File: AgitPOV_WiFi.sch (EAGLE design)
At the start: 43 parts, among them U1 MMA8452Q

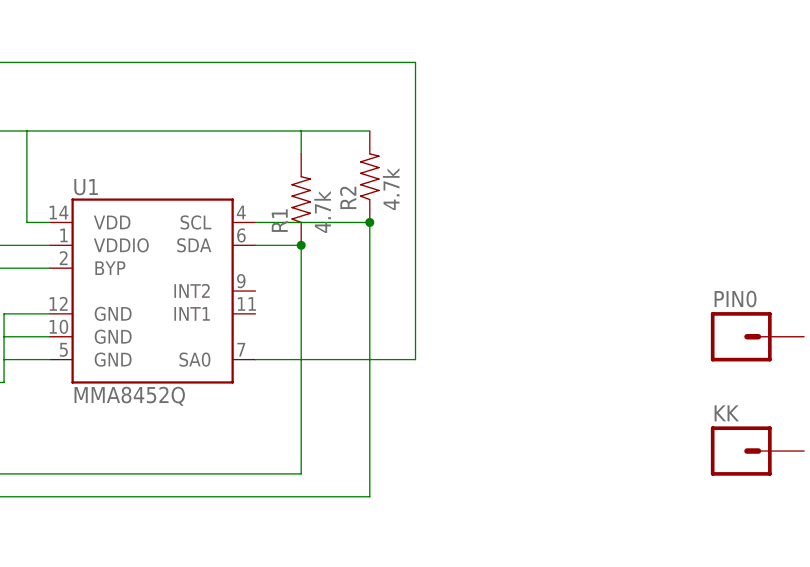
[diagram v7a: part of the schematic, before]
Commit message: Added pin headers for INT1 and INT2
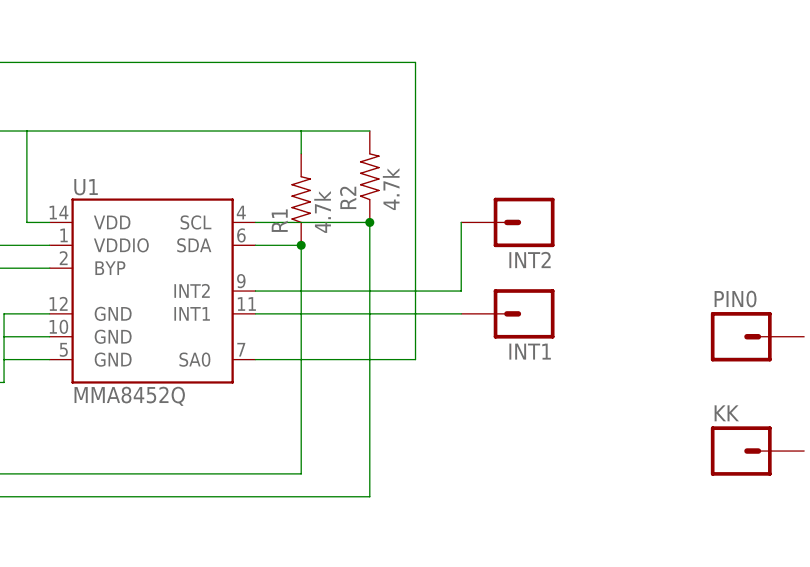
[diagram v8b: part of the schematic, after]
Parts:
- added INT1, INT2: (no value), SparkFun-Connectors:M01PTH
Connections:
- new net N$65: INT1.1, U1.INT1
- new net N$67: INT2.1, U1.INT2
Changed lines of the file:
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@@
 <part name="U1" library="SparkFun-Sensors" deviceset="MMA8452Q" device=""/>
 <part name="C3" library="SparkFun-Capacitors" deviceset="10UF-16V-10%(TANT)" device="" value="4.7uF"/>
+<part name="INT1" library="SparkFun-Connectors" deviceset="M01" device="PTH"/>
+<part name="INT2" library="SparkFun-Connectors" deviceset="M01" device="PTH"/>
 </parts>
 <sheets>
@@
 <instance part="U1" gate="G$1" x="127" y="43.18"/>
 <instance part="C3" gate="G$1" x="81.28" y="40.64"/>
+<instance part="INT1" gate="G$1" x="170.18" y="40.64" rot="R180"/>
+<instance part="INT2" gate="G$1" x="170.18" y="50.8" rot="R180"/>
 </instances>
 <busses>
@@
 </segment>
 </net>
+<net name="N$65" class="0">
+<segment>
+<pinref part="U1" gate="G$1" pin="INT1"/>
+<pinref part="INT1" gate="G$1" pin="1"/>
+<wire x1="139.7" y1="40.64" x2="162.56" y2="40.64" width="0.1524" layer="91"/>
+</segment>
+</net>
+<net name="N$67" class="0">
+<segment>
+<pinref part="U1" gate="G$1" pin="INT2"/>
+<pinref part="INT2" gate="G$1" pin="1"/>
+<wire x1="139.7" y1="43.18" x2="162.56" y2="43.18" width="0.1524" layer="91"/>
+<wire x1="162.56" y1="43.18" x2="162.56" y2="50.8" width="0.1524" layer="91"/>
+</segment>
+</net>
